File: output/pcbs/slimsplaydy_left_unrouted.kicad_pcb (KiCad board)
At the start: 2 copper layers, 117.1 x 87.4 mm, 24 parts

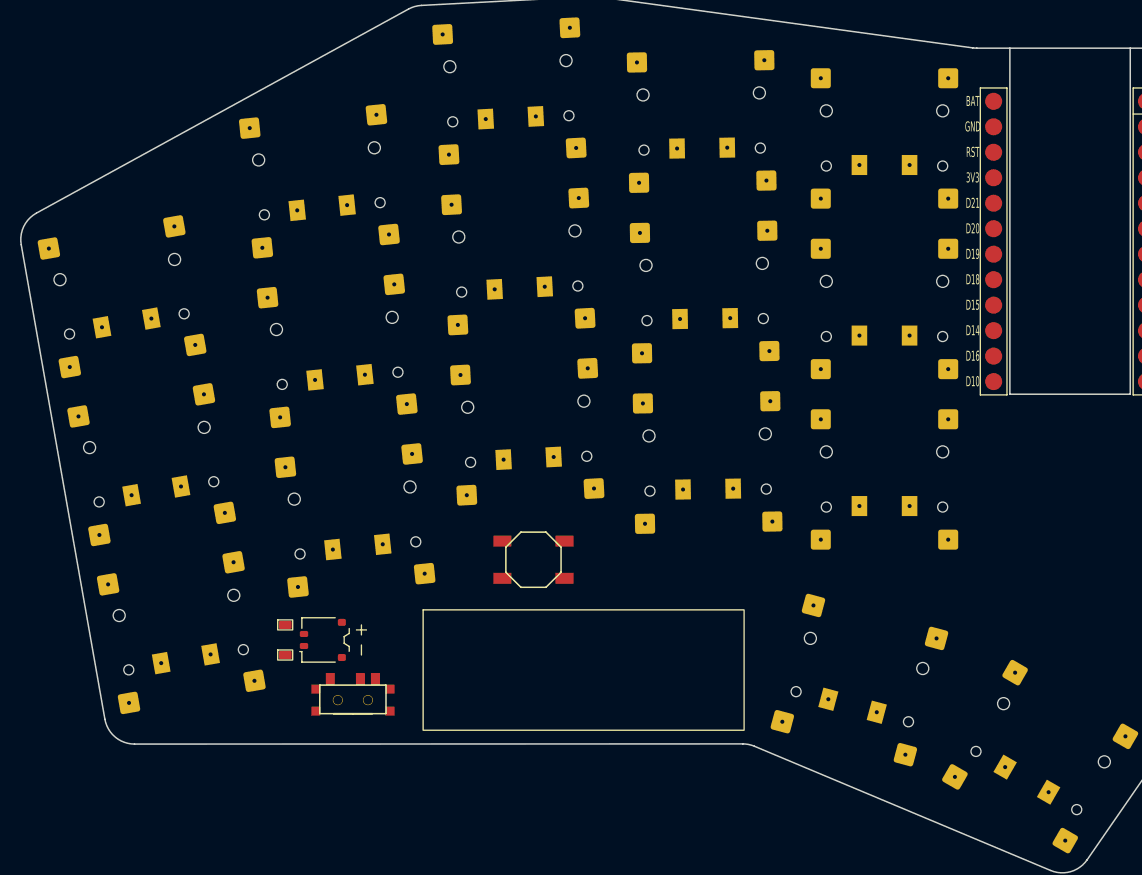
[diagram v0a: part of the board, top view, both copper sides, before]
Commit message: Add logic to only place vias once when board is reversible; fix mispellings of reversible.
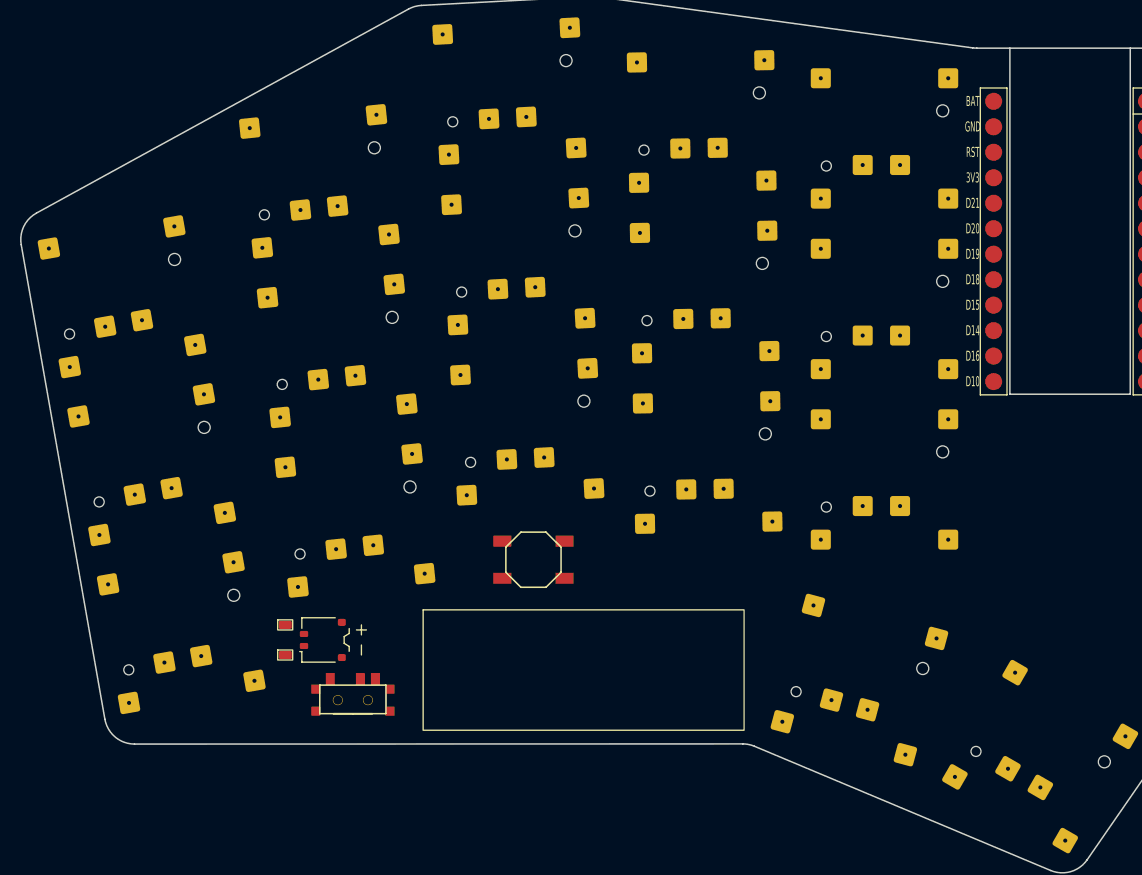
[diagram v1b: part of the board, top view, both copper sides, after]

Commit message: Reposition battery/connector, work on mounting holes.
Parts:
- removed B1: , E73:SW_TACT_ALPS_SKQGABE010
- removed T1: , E73:SPDT_C128955
- removed XX2: , Pad_Single
- removed XX3: , Battery_301230
- added MH1: , ceoloide:mounting_hole_npth, F.Cu at (179.0, 81.4)
- added MH10: , ceoloide:mounting_hole_npth, F.Cu at (168.0, 135.2)
- added MH11: , ceoloide:mounting_hole_npth, F.Cu at (150.9, 132.1)
- added MH12: , ceoloide:mounting_hole_npth, F.Cu at (137.1, 132.8)
- added MH13: , ceoloide:mounting_hole_npth, F.Cu at (129.9, 154.6)
- added MH14: , ceoloide:mounting_hole_npth, F.Cu at (101.0, 154.1)
- added MH15: , ceoloide:mounting_hole_npth, F.Cu at (95.3, 127.1)
- added MH16: , ceoloide:mounting_hole_npth, F.Cu at (90.4, 100.6)
- added MH17: , ceoloide:mounting_hole_npth, F.Cu at (110.9, 90.2)
- added MH18: , ceoloide:mounting_hole_npth, F.Cu at (130.1, 79.1)
- added MH19: , ceoloide:mounting_hole_npth, F.Cu at (152.1, 78.0)
- added MH2: , ceoloide:mounting_hole_npth, F.Cu at (208.8, 86.2)
- added MH3: , ceoloide:mounting_hole_npth, F.Cu at (190.0, 119.2)
- added MH4: , ceoloide:mounting_hole_npth, F.Cu at (207.0, 119.2)
- added MH5: , ceoloide:mounting_hole_npth, F.Cu at (192.0, 136.2)
- added MH6: , ceoloide:mounting_hole_npth, F.Cu at (207.0, 147.2)
- added MH7: , ceoloide:mounting_hole_npth, F.Cu at (197.9, 168.0)
- added MH8: , ceoloide:mounting_hole_npth, F.Cu at (173.6, 157.0)
- added MH9: , ceoloide:mounting_hole_npth, F.Cu at (163.3, 153.0)
- added PAD1: , SMDPad, F.Cu at (139.2, 135.2)
- added PAD2: , SMDPad, F.Cu at (139.5, 138.2)
- added PWR1: , ceoloide:power_switch_smd_side, F.Cu at (209.0, 138.2)
- added RST1: , ceoloide:reset_switch_smd_side, F.Cu at (209.0, 128.2)
- XX1: footprint Pad_Single -> Battery_301230
- moved XX1 30.1 mm to (147.0, 145.2), turned to 6 degrees
- moved CONN1 23.7 mm to (143.0, 136.2), turned to 96 degrees
- moved MCU1 5.30 mm to (197.5, 98.6)
- moved S9 3.17 mm to (141.6, 87.5)
- moved S7 3.17 mm to (143.4, 121.5)
- moved S8 3.17 mm to (142.5, 104.5)
- moved S11 3.17 mm to (161.0, 107.5)
- moved S10 3.17 mm to (161.3, 124.5)
- moved S4 3.17 mm to (126.2, 130.3)
- moved S5 3.17 mm to (124.4, 113.4)
- moved S12 3.17 mm to (160.7, 90.5)
- moved S15 3.17 mm to (179.0, 92.2)
- moved S13 3.17 mm to (179.0, 126.2)
- moved S14 3.17 mm to (179.0, 109.2)
- moved S16 3.17 mm to (176.5, 146.2)
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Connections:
- MCU1 pad 24: BAT -> RAW
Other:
- board size 117.1 x 87.4 mm -> 260.5 x 94.7 mm

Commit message: Finish up mounting, add case outlines, export step.
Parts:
- added MH20: , ceoloide:mounting_hole_npth, F.Cu at (5.05, -28.0)
- moved MH14 203.8 mm to (-13.3, -14.7)
- moved MH15 200.4 mm to (-17.8, -38.3)
- moved MH10 199.3 mm to (29.4, -8.05), turned to 3 degrees
- moved MH13 199.0 mm to (-8.20, 11.3)
- moved MH7 195.4 mm to (72.6, 18.0), turned to -15 degrees
- moved MH11 190.7 mm to (12.4, 1.08), turned to 6 degrees
- moved MH9 190.4 mm to (57.9, -5.57), turned to 0 degrees
- moved MH8 190.2 mm to (53.0, 9.89)
- moved XX1 179.8 mm to (37.7, 2.45)
- moved RST1 179.7 mm to (99.9, -14.6)
- moved S17 178.9 mm to (85.4, 12.1)
- moved S12 178.9 mm to (51.7, -51.3)
- moved S11 178.9 mm to (52.0, -34.3)
- moved S4 178.9 mm to (17.1, -11.5)
- moved S5 178.9 mm to (15.3, -28.4)
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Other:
- board size 260.5 x 94.7 mm -> 122.3 x 94.4 mm
- net class Default removed

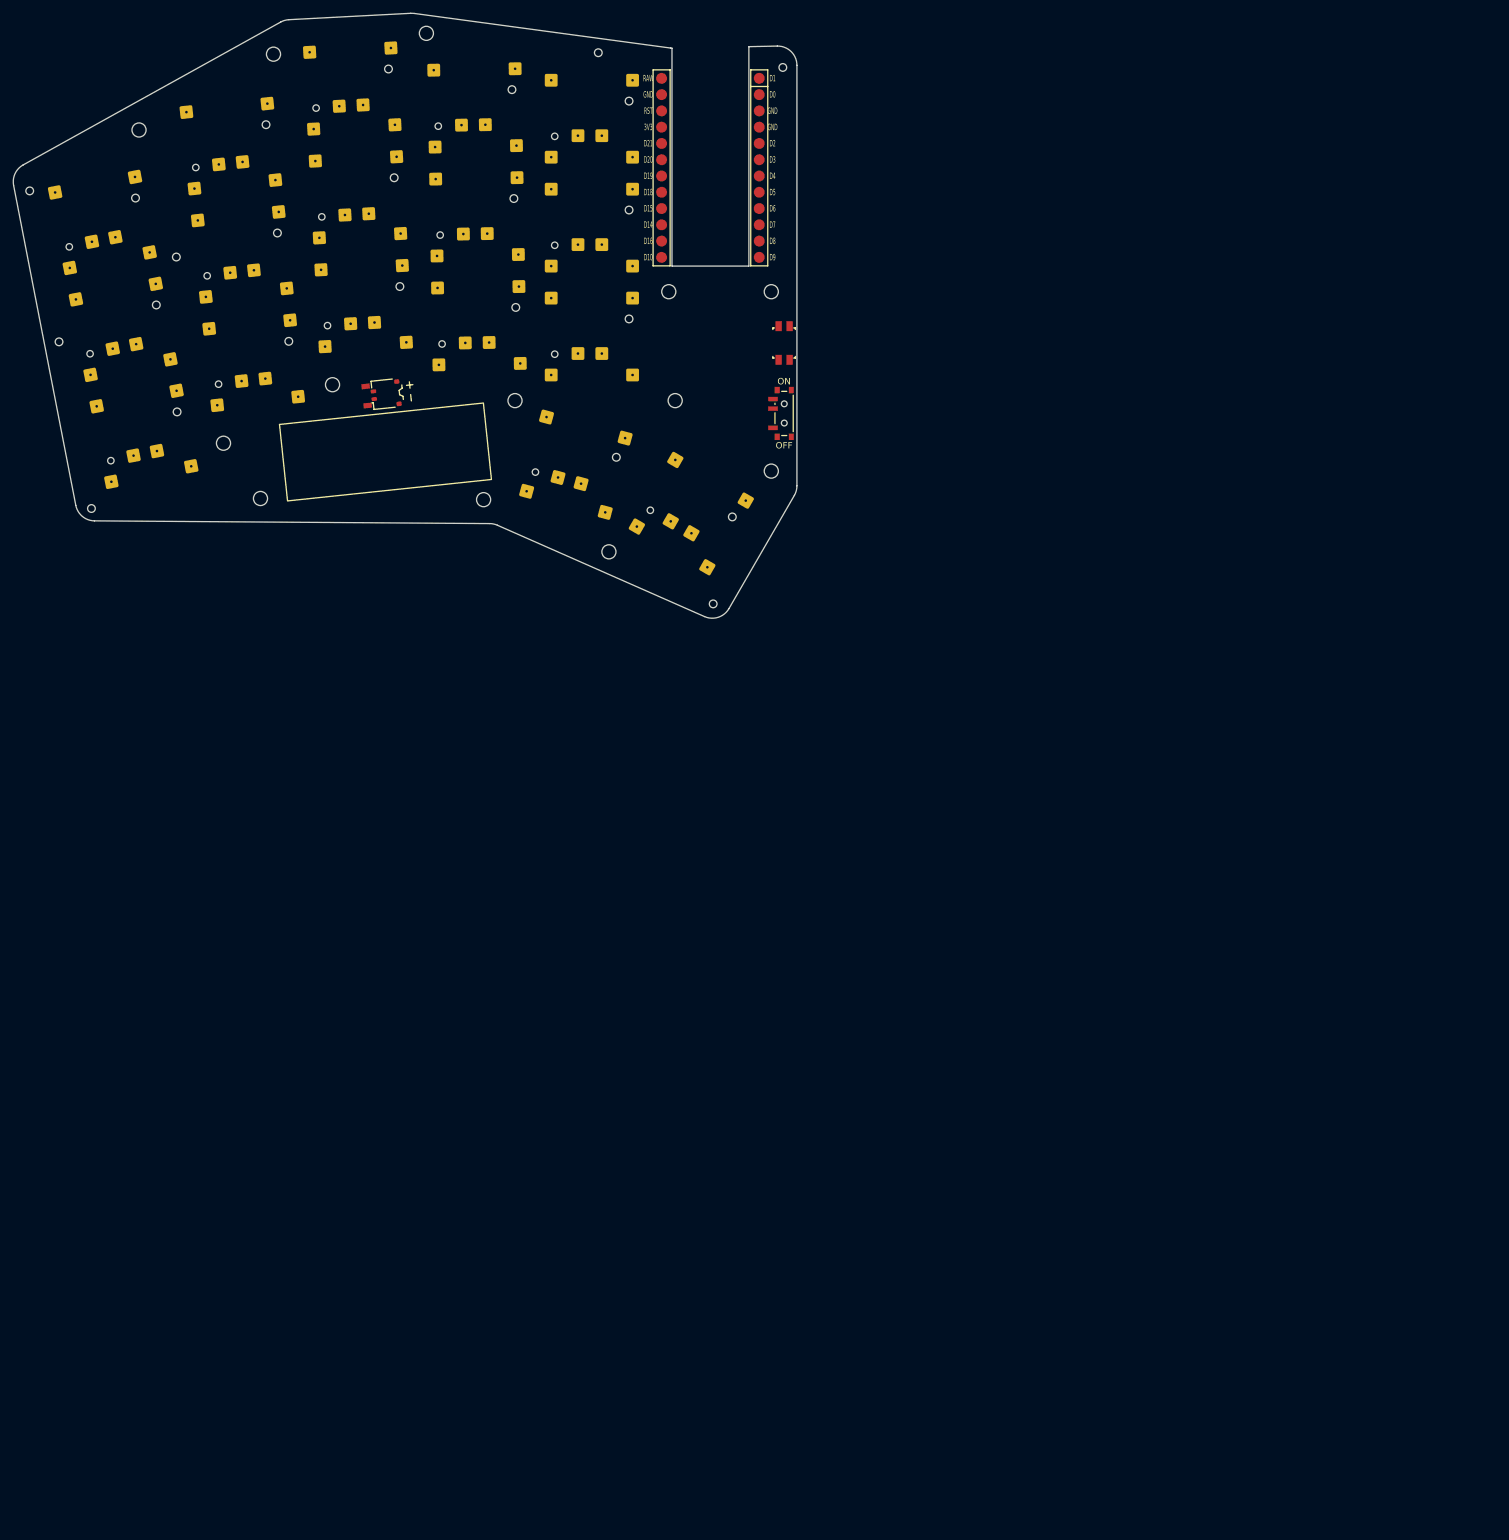
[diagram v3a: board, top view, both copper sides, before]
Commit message: Fix bug in PG1316S footprint causing vias in pads to not route correctly.
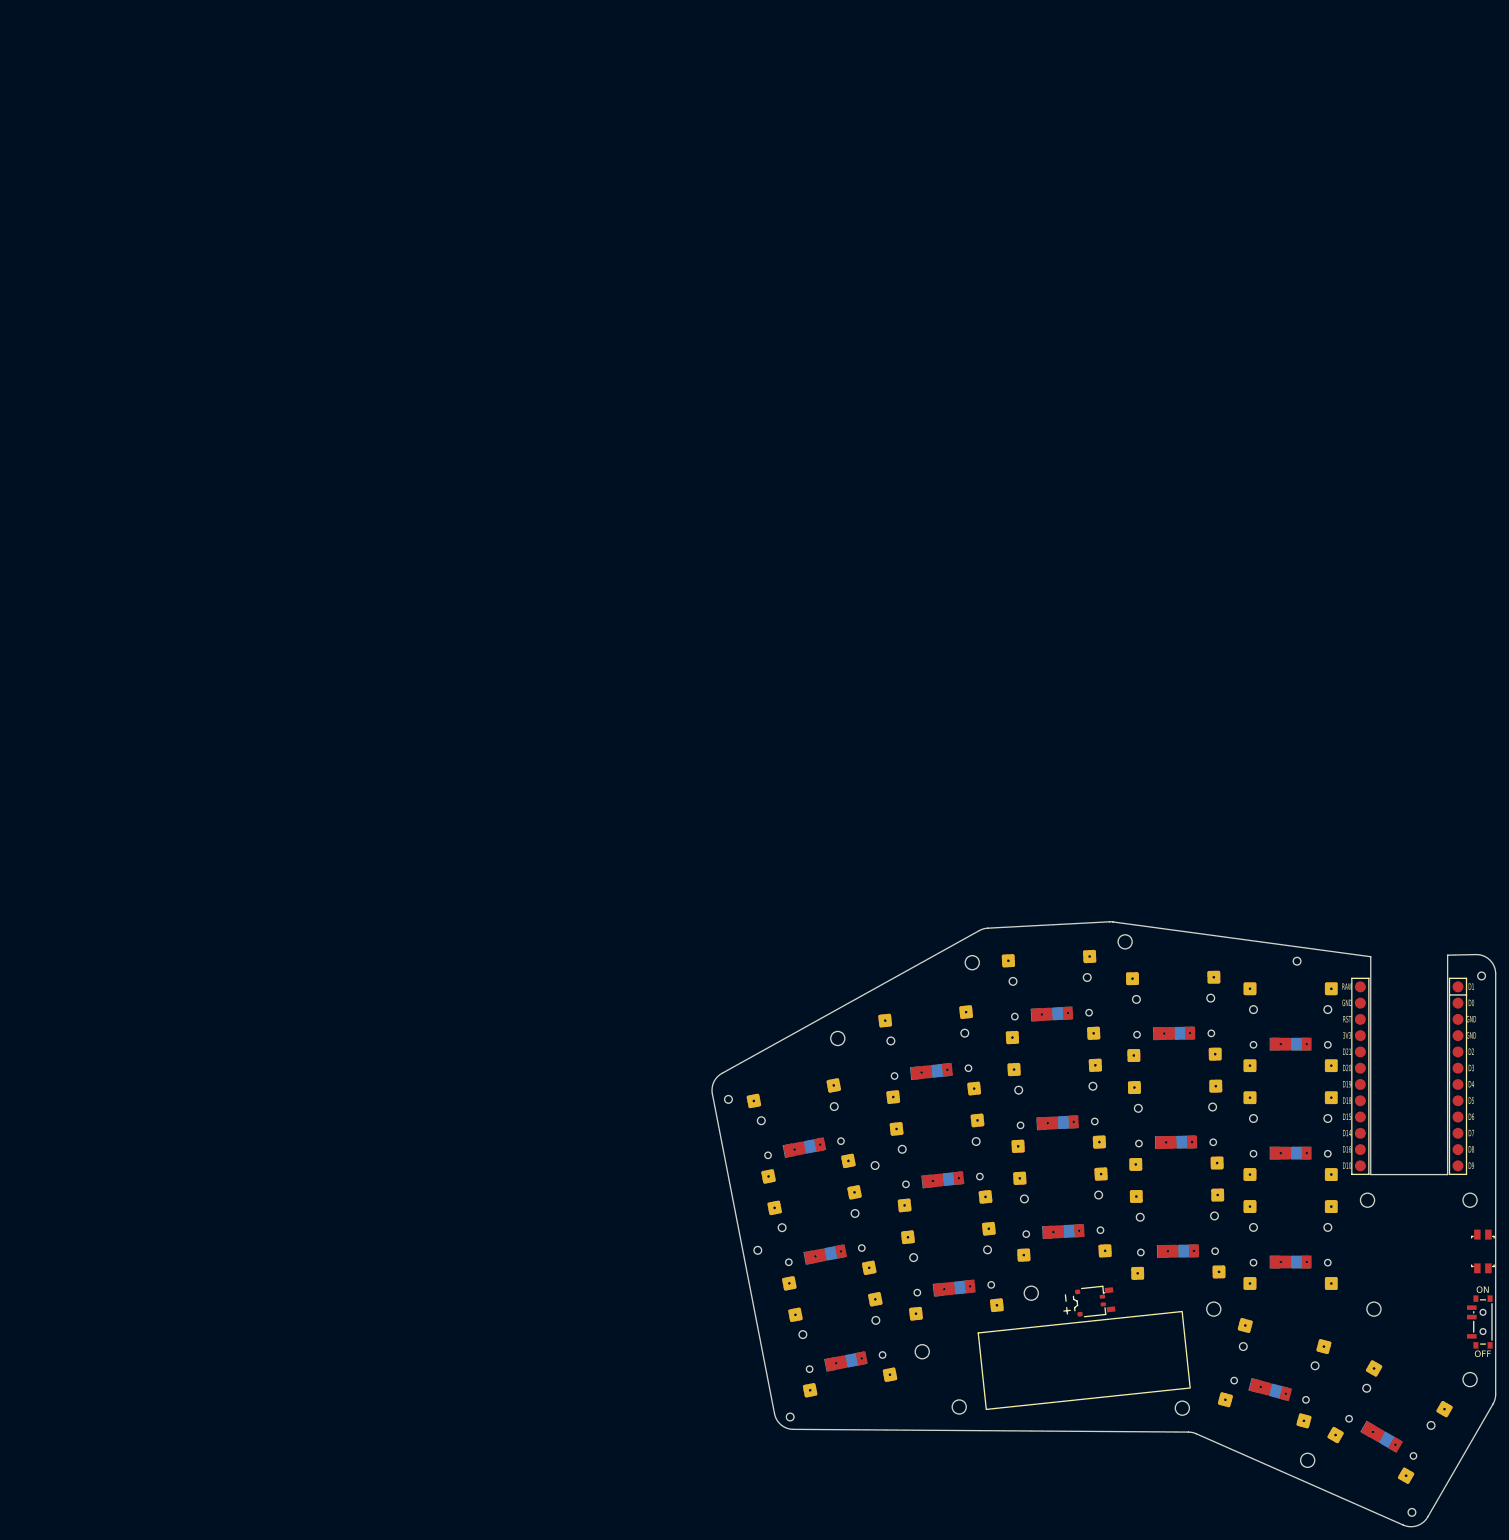
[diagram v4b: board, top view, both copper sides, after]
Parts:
- moved PAD1 185.2 mm to (150.9, 136.3)
- moved PAD2 180.2 mm to (150.6, 133.3)
- moved CONN1 179.4 mm to (147.8, 135.1), turned to -84 degrees
- moved MH6 178.9 mm to (197.9, 168.0)
- moved S17 178.9 mm to (194.5, 153.9)
- moved S12 178.9 mm to (160.7, 90.5)
- moved MH10 178.9 mm to (138.5, 133.7)
- moved MH11 178.9 mm to (121.5, 142.9)
- moved S11 178.9 mm to (161.0, 107.5)
- moved S4 178.9 mm to (126.2, 130.3)
- moved S5 178.9 mm to (124.4, 113.4)
- moved XX1 178.9 mm to (146.8, 144.2)
- moved S7 178.9 mm to (143.4, 121.5)
- moved MH1 178.9 mm to (208.8, 84.2)
- moved MCU1 178.9 mm to (197.5, 98.6)
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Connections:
- S1 pad 3: (no net) -> GND
- S10 pad 3: (no net) -> GND
- S11 pad 3: (no net) -> GND
- S12 pad 3: (no net) -> GND
- S13 pad 3: (no net) -> GND
- S14 pad 3: (no net) -> GND
- S15 pad 3: (no net) -> GND
- S16 pad 3: (no net) -> GND
- S17 pad 3: (no net) -> GND
- S2 pad 3: (no net) -> GND
- S3 pad 3: (no net) -> GND
- S4 pad 3: (no net) -> GND
- S5 pad 3: (no net) -> GND
- S6 pad 3: (no net) -> GND
- S7 pad 3: (no net) -> GND
- S8 pad 3: (no net) -> GND
- S9 pad 3: (no net) -> GND

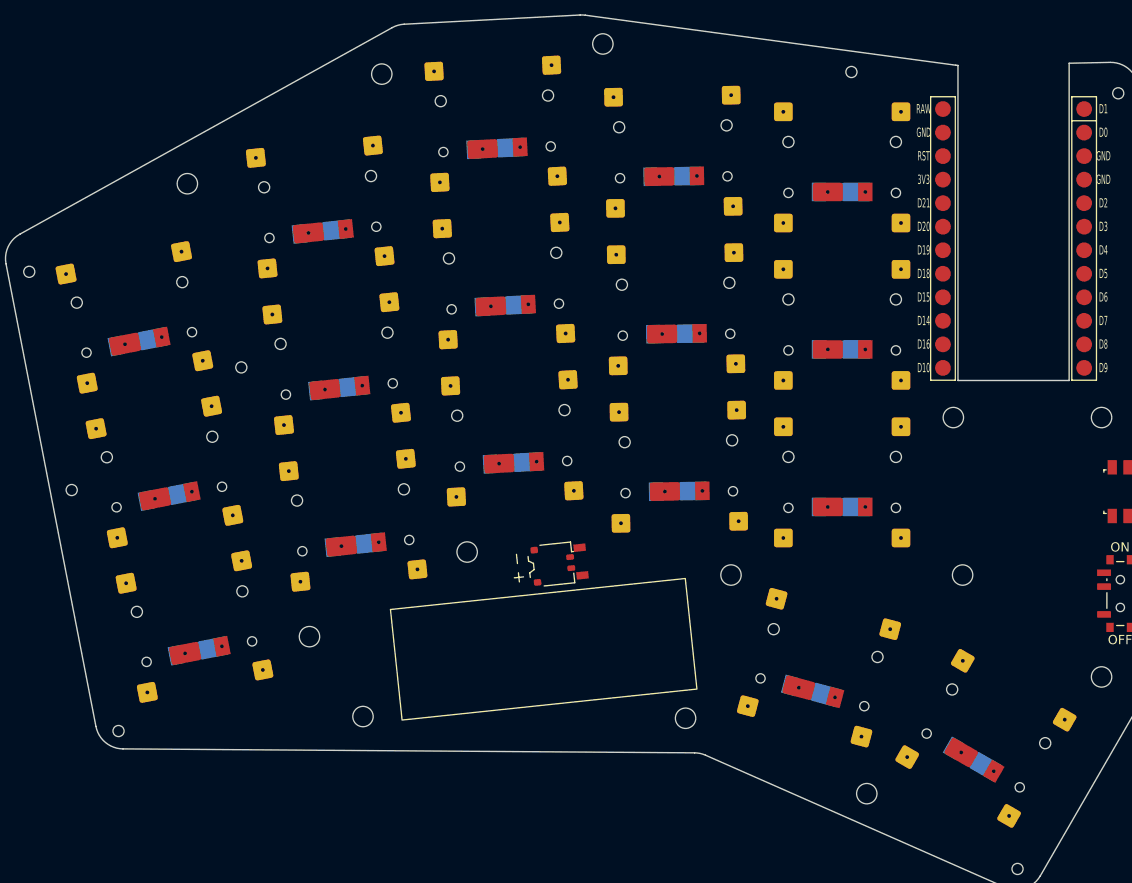
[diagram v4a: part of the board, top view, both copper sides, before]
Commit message: Add via holesize options separate from via size options.
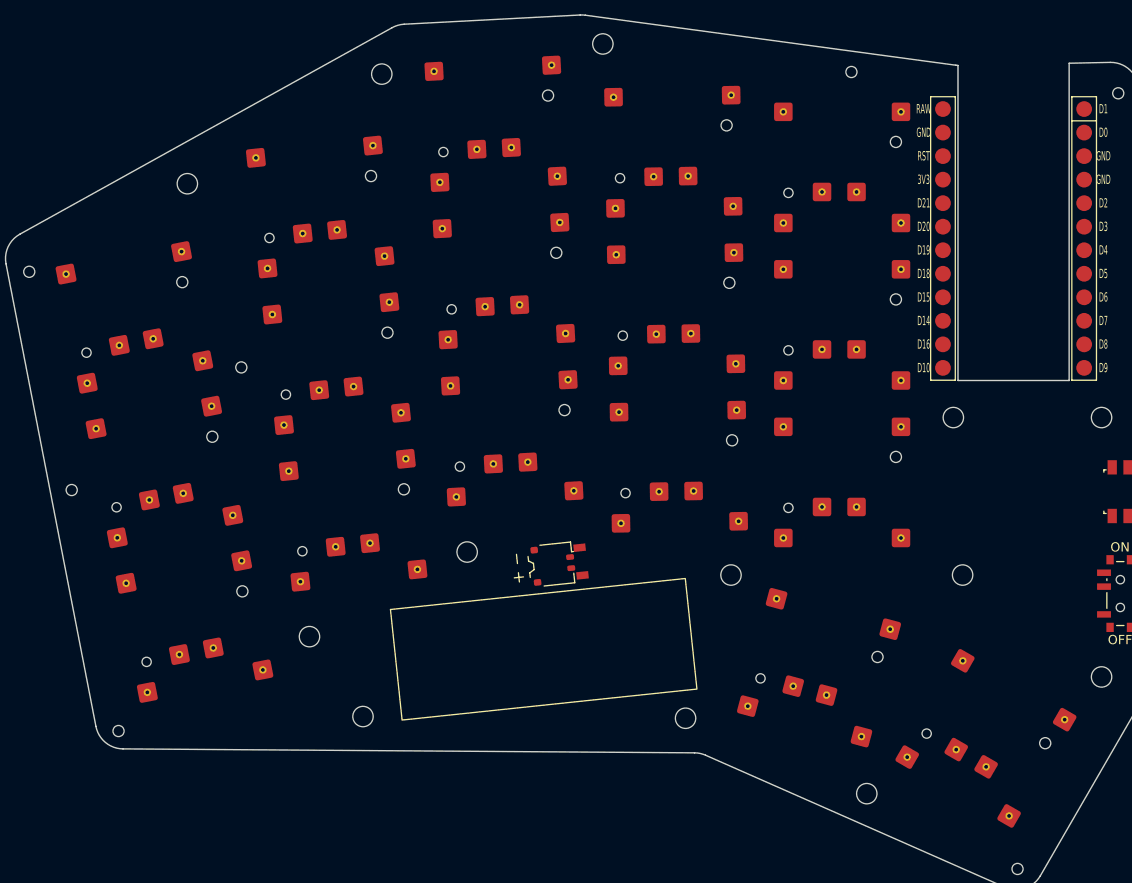
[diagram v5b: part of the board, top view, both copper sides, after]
